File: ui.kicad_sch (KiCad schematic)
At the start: 4 parts

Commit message: Wire more stuff
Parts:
- removed D1, D2: LED, symbol Device:LED
- removed R4: R, symbol Device:R
- added D1: LED_RGBK, symbol Device:LED_RGBK
- added R20: R_{LED_PORT0.G}, symbol Device:R
- added R21: R_{LED_PORT0.B}, symbol Device:R
- R3: value R -> R_{LED_PORT0.R}
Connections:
- net GND: now also D1.4 (K); no longer R3.1
- net LED_PORT0.R: now reaches R3.2
- new net: D1.3 (BA), R21.1
- new net: D1.1 (RA), R3.1
- new net: D1.2 (GA), R20.1
- new net LED_PORT0.B: R21.2
- new net LED_PORT0.G: R20.2
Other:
- note added: "For LED, could use something like this: https://www.adafruit.com/product/2739"
- note added: "Use light guide / light pipe to make round 5mm RGB LED look like a rectangle"
- note removed: "Fit LEDs on PCB edge? RGB to indicate voltage maybe?"

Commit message: Whole bunch of changes to all kinds of things
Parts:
- removed D1: LED_RGBK, symbol Device:LED_RGBK
- removed R20: R_{LED_PORT0.G}, symbol Device:R
- removed R21: R_{LED_PORT0.B}, symbol Device:R
- added D2: L-119EGWT, symbol Device:LED_Dual_AKA
- added R25: R_{LED_PORT0.R}, symbol Device:R
- added R27: R_{LED_PORT0.G}, symbol Device:R
- added SW1: TS-1187A-B-A-B, symbol Switch:SW_Push
- R3: value R_{LED_PORT0.R} -> 10k
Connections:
- net GND: now also D2.2 (K), SW1.2
- net LED_PORT0.G: now also R27.2
- net LED_PORT0.R: now also R25.2; no longer R3.2
- net +3V3: now reaches R3.1
- new net: D2.3 (A2), R25.1
- new net: D2.1 (A1), R27.1
- new net ~{RESET}: R3.2, SW1.1
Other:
- note removed: "For LED, could use something like this: https://www.adafruit.com/product/2739"
- note removed: "Use light guide / light pipe to make round 5mm RGB LED look like a rectangle"

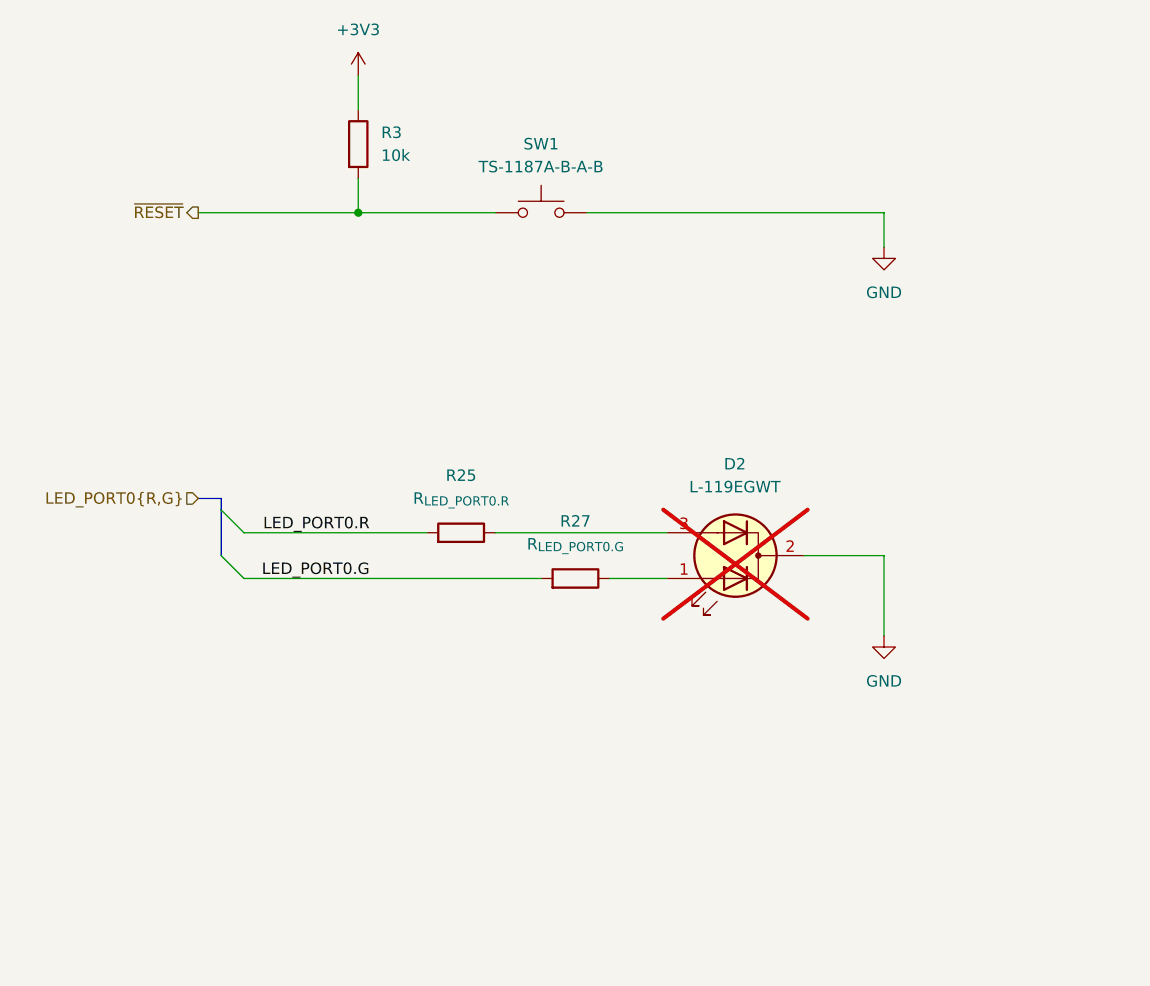
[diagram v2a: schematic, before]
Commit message: wire up vconn stuff
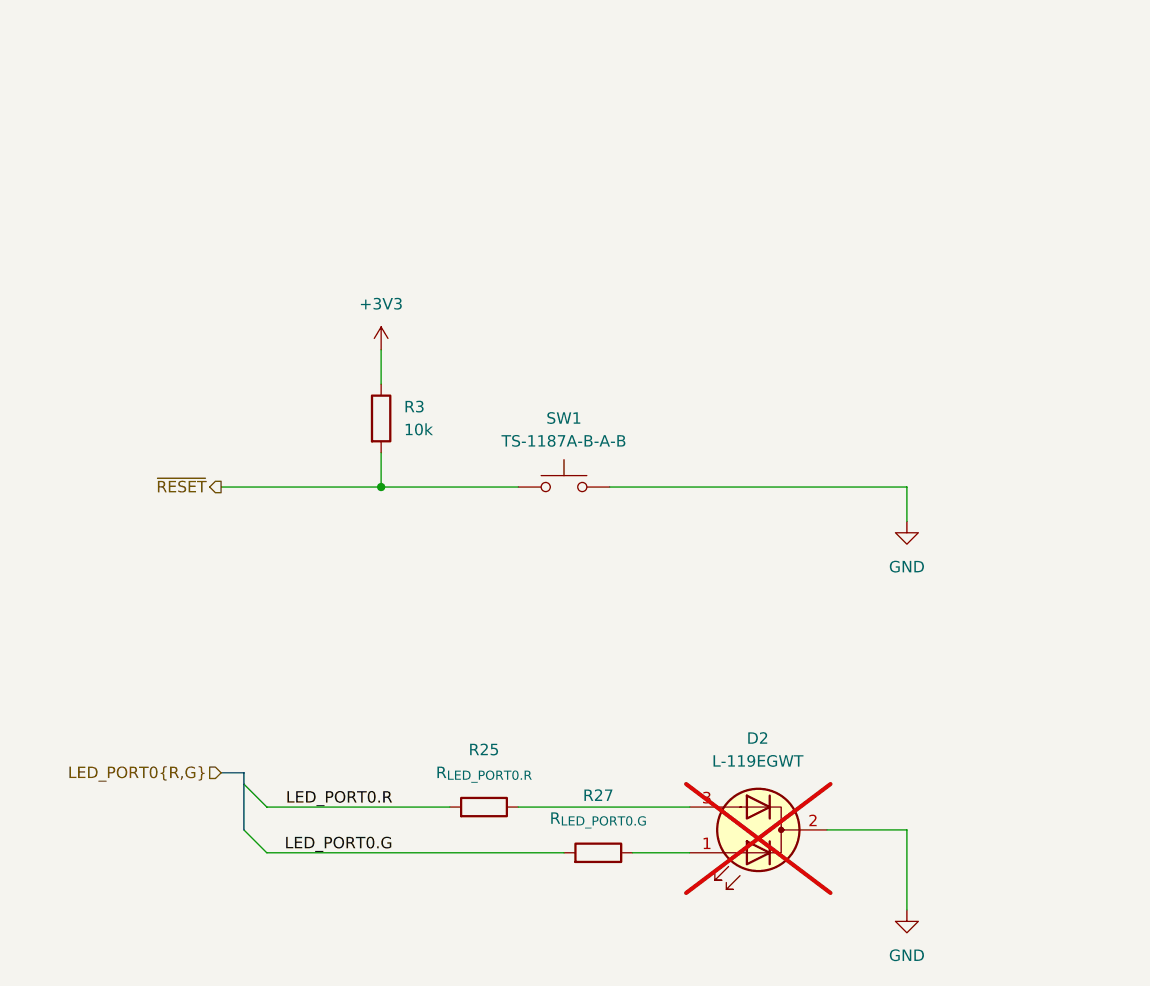
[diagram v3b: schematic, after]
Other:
- moved on the sheet: D2, R25, R27, R3, SW1

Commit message: more footprints
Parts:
- D2: footprint (none) -> Connector_PinHeader_2.54mm:PinHeader_1x03_P2.54mm_Vertical
- R3: footprint (none) -> Resistor_SMD:R_1206_3216Metric; JLCPCB Part No (none) -> C17902
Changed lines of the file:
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@@
 			)
 		)
-		(property "Footprint" ""
+		(property "Footprint" "Connector_PinHeader_2.54mm:PinHeader_1x03_P2.54mm_Vertical"
 			(at 171.45 114.3 0)
 			(effects
@@
 			)
 		)
-		(property "Footprint" ""
+		(property "Footprint" "Resistor_SMD:R_1206_3216Metric"
 			(at 127.762 68.58 90)
 			(effects
@@
 			)
 		)
-		(property "JLCPCB Part No" ""
-			(at 129.54 68.58 0)
-			(effects
+		(property "JLCPCB Part No" "C17902"
+			(at 129.54 68.58 0)
+			(effects
